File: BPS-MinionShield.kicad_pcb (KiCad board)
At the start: 2 copper layers, 85 x 66 mm, 91 parts, among them J1 TempConn1, J2 TempConn2, J3 Conn_01x24_Female, T1 TestPoint, T10 TestPoint, T11 TestPoint, T12 TestPoint, T13 TestPoint, T14 TestPoint, T15 TestPoint, T16 TestPoint, T2 TestPoint, T3 TestPoint, T4 TestPoint, T5 TestPoint, T6 TestPoint, T7 TestPoint, T8 TestPoint, T9 TestPoint

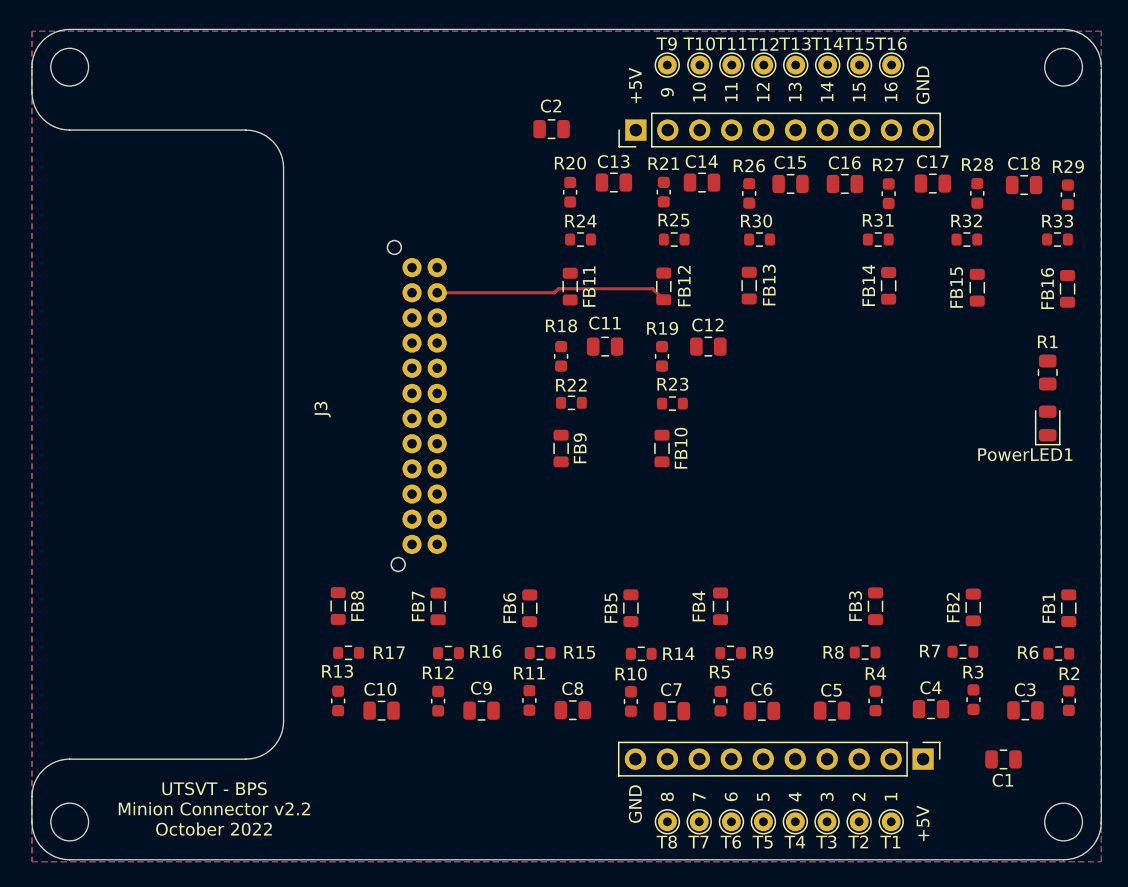
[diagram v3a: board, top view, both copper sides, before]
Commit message: pcb routing done
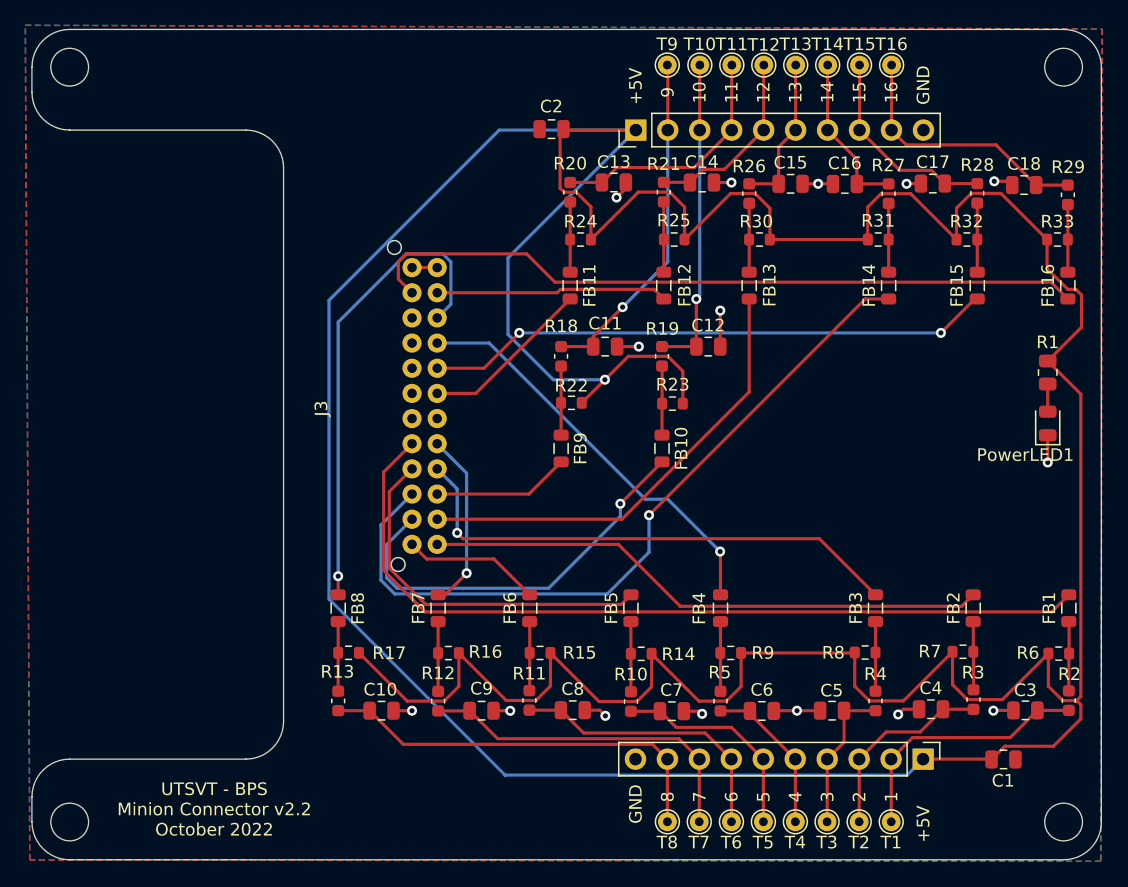
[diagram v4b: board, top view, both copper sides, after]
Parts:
- moved FB16 0.26 mm to (182.3, 90.4), turned to -90 degrees
- moved FB15 0.17 mm to (175.1, 90.4)
- moved FB8 0.17 mm to (124.3, 116.0)
- moved FB3 0.15 mm to (167.1, 116.0)
- moved FB4 0.14 mm to (154.7, 116.0)
- moved FB7 0.14 mm to (132.3, 116.0)
- moved FB11 0.08 mm to (142.8, 90.4)
- moved FB12 0.07 mm to (150.2, 90.4)
- moved FB2 0.06 mm to (174.8, 116.0)
- turned C15 to 180 degrees
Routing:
- net +5V: track 0.18 -> 364.6 mm, vias 0 -> 1
- net /temp1: track 0.00 -> 67.4 mm
- net /temp8: track 0.00 -> 60.1 mm, vias 0 -> 1
- net /temp16: track 0.00 -> 57.9 mm
- net /temp12: track 0.00 -> 45.2 mm, vias 0 -> 2
- net /temp5: track 0.00 -> 45.0 mm
- net /temp9: track 0.00 -> 41.0 mm, vias 0 -> 1
- net /temp14: track 0.00 -> 38.0 mm, vias 0 -> 1
- net /temp4: track 0.00 -> 36.4 mm
- net /temp13: track 0.00 -> 32.8 mm, vias 0 -> 1
- net /TempSens8: track 0.00 -> 32.7 mm
- net /temp7: track 0.00 -> 32.5 mm, vias 0 -> 1
- net GND: track 0.00 -> 30.1 mm, vias 0 -> 15
- net /temp2: track 0.00 -> 29.4 mm
- net /TempSens9: track 0.00 -> 27.4 mm, vias 0 -> 1
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- added copper zone on F.Cu, net GND
- removed copper zone on F.Cu, net +5V
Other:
- outline, holes or cut-outs redrawn

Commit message: generated BOM
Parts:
- added GND: TestPoint, TestPoint:TestPoint_THTPad_D1.5mm_Drill0.7mm, F.Cu at (173.3, 72.8)
- added GND: TestPoint, TestPoint:TestPoint_THTPad_D1.5mm_Drill0.7mm, F.Cu at (145.5, 133.0)

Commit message: made stuff pretty and rerouted
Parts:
- added FB17: 2.2k, Inductor_SMD:L_0805_2012Metric, F.Cu at (136.1, 91.9)
- added FB18: 2.2k, Inductor_SMD:L_0805_2012Metric, F.Cu at (136.1, 103.9)
- added GND: TestPoint, TestPoint:TestPoint_THTPad_D1.5mm_Drill0.7mm, F.Cu at (140.6, 105.4)
- added GND: TestPoint, TestPoint:TestPoint_THTPad_D1.5mm_Drill0.7mm, F.Cu at (137.2, 88.5)
- added GND: TestPoint, TestPoint:TestPoint_THTPad_D1.5mm_Drill0.7mm, F.Cu at (165.1, 105.3)
- moved FB10 24.3 mm to (132.4, 86.7)
- moved FB9 24.3 mm to (124.3, 86.7)
- moved R18 24.3 mm to (124.3, 79.3)
- moved R19 24.3 mm to (132.4, 79.3)
- moved R22 24.3 mm to (125.2, 83.0)
- moved C11 24.3 mm to (127.8, 78.6)
- moved C12 24.3 mm to (136.0, 78.6)
- moved R23 24.3 mm to (133.2, 83.1)
- moved FB7 2.92 mm to (132.3, 118.9)
- moved FB8 2.92 mm to (124.3, 118.9)
- moved R12 2.92 mm to (132.3, 126.3)
- moved R13 2.92 mm to (124.3, 126.3)
- moved R16 2.92 mm to (133.1, 122.5)
- moved R17 2.92 mm to (125.2, 122.5)
- moved C10 2.92 mm to (127.8, 127.1)
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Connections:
- J3 pad 1: GND -> Net-(J3-Pad1)
- J3 pad 13: GND -> Net-(J3-Pad13)
- J3 pad 14: GND -> Net-(J3-Pad13)
- J3 pad 2: GND -> Net-(J3-Pad1)
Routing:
- net +5V: track 364.6 -> 233.2 mm, vias 1 -> 0
- net /temp3: track 10.9 -> 41.5 mm
- net GND: track 30.1 -> 22.1 mm, vias 15 -> 12
- net /temp4: track 36.4 -> 44.1 mm, vias 0 -> 1
- net /temp8: track 60.1 -> 67.0 mm
- net /temp7: track 32.5 -> 25.9 mm, vias 1 -> 0
- net /temp11: track 13.7 -> 19.9 mm, vias 0 -> 1
- net /TempSens9: track 27.4 -> 33.4 mm
- net /temp13: track 32.8 -> 38.4 mm
- net Net-(J3-Pad1): track 0.00 -> 4.84 mm
- net Net-(J3-Pad13): track 0.00 -> 4.83 mm
- net /temp12: track 45.2 -> 49.9 mm, vias 2 -> 1
- net /temp14: track 38.0 -> 34.3 mm, vias 1 -> 0
- net /TempSens10: track 25.2 -> 28.0 mm
- net /temp2: track 29.4 -> 31.5 mm, vias 0 -> 1
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
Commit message: redid the vias
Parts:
- removed C17: 1u, Capacitor_SMD:C_0805_2012Metric
- removed T1, T10, T11, T12, T13, T14, T15, T16, T2, T3, T4, T5, T6, T7, T8, T9: TestPoint, TestPoint:TestPoint_THTPad_D1.5mm_Drill0.7mm
- moved GND1 3.59 mm to (142.2, 131.6)
- moved GND2 1.64 mm to (173.4, 74.3)
- moved R7 0.09 mm to (174.0, 119.6)
- moved R22 0.06 mm to (125.2, 83.1)
- renumbered GND to GND1, GND to GND2, GND to GND3, GND to GND4, GND to GND5
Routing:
- net GND: track 22.1 -> 5.04 mm, vias 12 -> 3
- net +5V: track 233.2 -> 217.0 mm, vias 0 -> 17
- net /TempSens13: track 12.3 -> 7.17 mm
- net /TempSens16: track 21.0 -> 15.8 mm
- net /TempSens14: track 12.9 -> 7.77 mm
- net /TempSens11: track 19.7 -> 14.6 mm
- net /TempSens10: track 28.0 -> 22.9 mm
- net /TempSens12: track 14.8 -> 9.67 mm
- net /TempSens15: track 16.3 -> 11.1 mm
- net /TempSens9: track 33.4 -> 28.3 mm
- net /TempSens1: track 20.7 -> 15.7 mm
- net /TempSens3: track 11.9 -> 6.91 mm
- net /TempSens4: track 12.6 -> 7.66 mm
- net /TempSens7: track 27.1 -> 22.2 mm
- net /TempSens5: track 17.1 -> 12.1 mm
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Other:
- board text removed: "9"

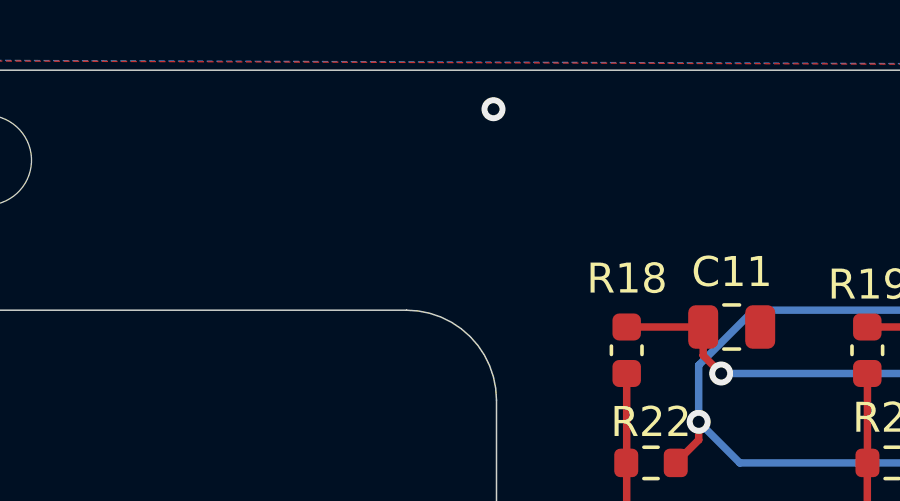
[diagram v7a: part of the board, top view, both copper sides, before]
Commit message: rerouted and added Dr. Hallock photo
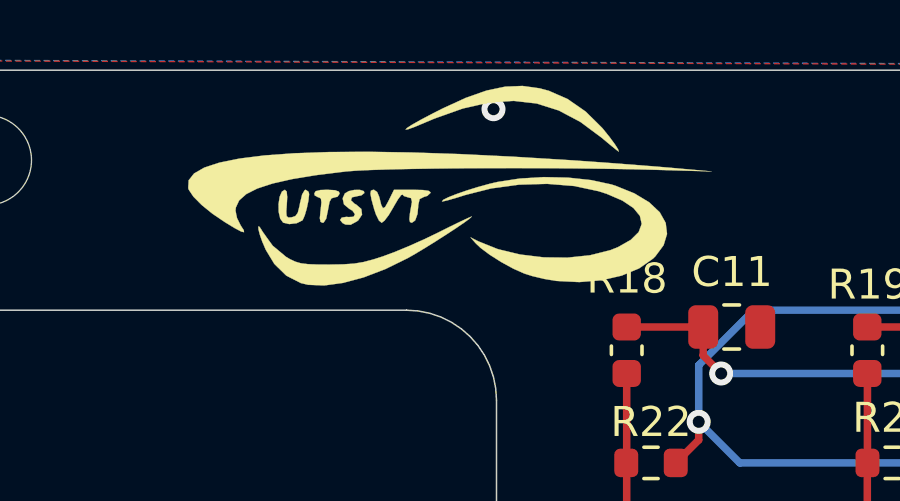
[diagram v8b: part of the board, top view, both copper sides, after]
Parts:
- added G***: LOGO, UTSVT_Special:UTSVT_Logo_Symbol, F.Cu at (118.2, 74.0)
- added G***: LOGO, UTSVT_Special:Hallock_Image_Tiny, B.Cu at (127.4, 125.5)
